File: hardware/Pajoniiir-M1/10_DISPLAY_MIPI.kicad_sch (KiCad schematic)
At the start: 30 parts

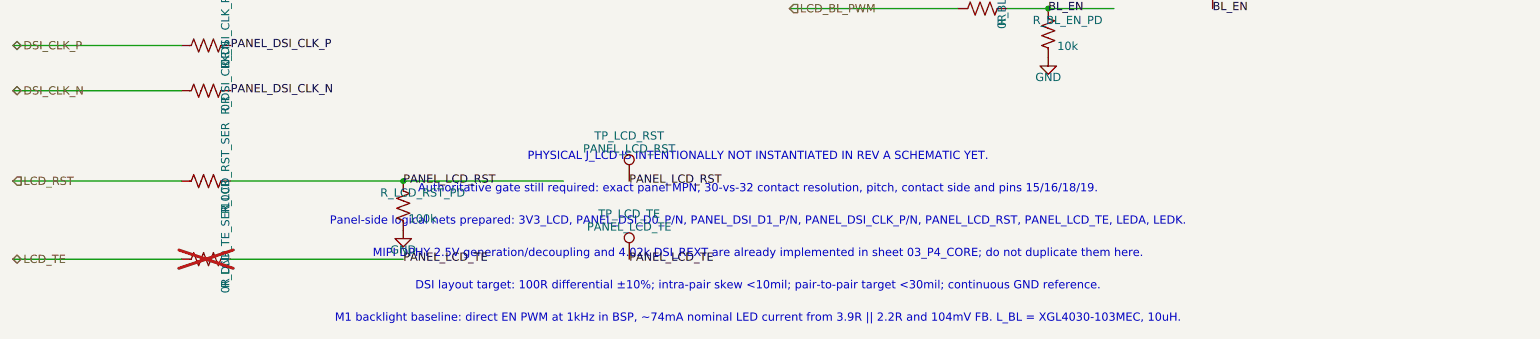
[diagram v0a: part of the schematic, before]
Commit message: hardware: record clean ERC and narrow display hard gate
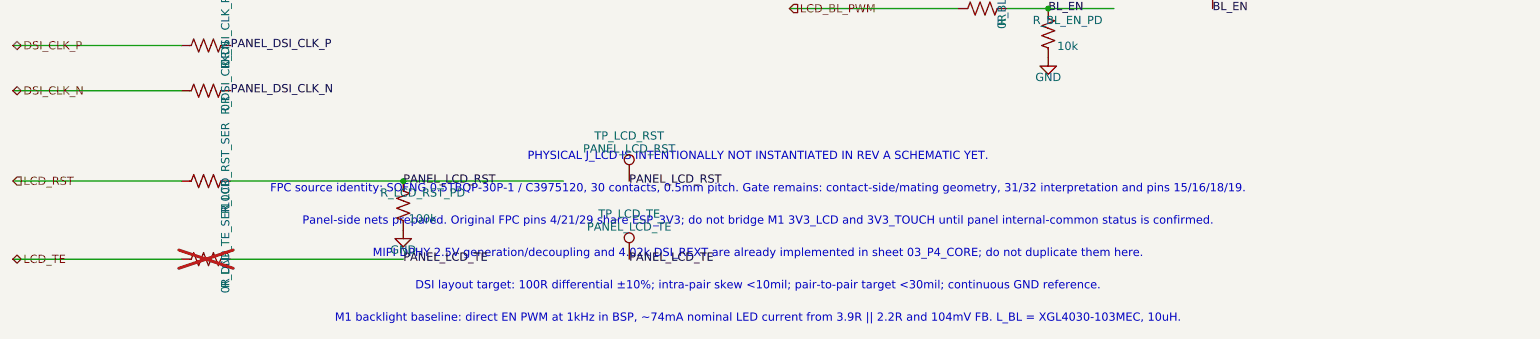
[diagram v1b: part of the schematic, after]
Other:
- note added: "FPC source identity: SOFNG 0.5TBQP-30P-1 / C3975120, 30 contacts, 0.5mm pitch. Gate remains: contact-side/mating geometry, 31/32 interpretation and pins 15/16/18/19."
- note added: "Panel-side nets prepared. Original FPC pins 4/21/29 share ESP_3V3; do not bridge M1 3V3_LCD and 3V3_TOUCH until panel internal-common status is confirmed."
- note removed: "Authoritative gate still required: exact panel MPN, 30-vs-32 contact resolution, pitch, contact side and pins 15/16/18/19."
- note removed: "Panel-side logical nets prepared: 3V3_LCD, PANEL_DSI_D0_P/N, PANEL_DSI_D1_P/N, PANEL_DSI_CLK_P/N, PANEL_LCD_RST, PANEL_LCD_TE, LEDA, LEDK."
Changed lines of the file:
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@@
   (label "BL_EN" (at 215.265 85.09 0) (effects (font (size 1.27 1.27))))
   (text "PHYSICAL J_LCD IS INTENTIONALLY NOT INSTANTIATED IN REV A SCHEMATIC YET." (exclude_from_sim no) (at 145 108 0) (effects (font (size 1.27 1.27))))
-  (text "Authoritative gate still required: exact panel MPN, 30-vs-32 contact resolution, pitch, contact side and pins 15/16/18/19." (exclude_from_sim no) (at 145 113 0) (effects (font (size 1.27 1.27))))
-  (text "Panel-side logical nets prepared: 3V3_LCD, PANEL_DSI_D0_P/N, PANEL_DSI_D1_P/N, PANEL_DSI_CLK_P/N, PANEL_LCD_RST, PANEL_LCD_TE, LEDA, LEDK." (exclude_from_sim no) (at 145 118 0) (effects (font (size 1.27 1.27))))
+  (text "FPC source identity: SOFNG 0.5TBQP-30P-1 / C3975120, 30 contacts, 0.5mm pitch. Gate remains: contact-side/mating geometry, 31/32 interpretation and pins 15/16/18/19." (exclude_from_sim no) (at 145 113 0) (effects (font (size 1.27 1.27))))
+  (text "Panel-side nets prepared. Original FPC pins 4/21/29 share ESP_3V3; do not bridge M1 3V3_LCD and 3V3_TOUCH until panel internal-common status is confirmed." (exclude_from_sim no) (at 145 118 0) (effects (font (size 1.27 1.27))))
   (text "MIPI DPHY 2.5V generation/decoupling and 4.02k DSI_REXT are already implemented in sheet 03_P4_CORE; do not duplicate them here." (exclude_from_sim no) (at 145 123 0) (effects (font (size 1.27 1.27))))
   (text "DSI layout target: 100R differential ±10%; intra-pair skew <10mil; pair-to-pair target <30mil; continuous GND reference." (exclude_from_sim no) (at 145 128 0) (effects (font (size 1.27 1.27))))

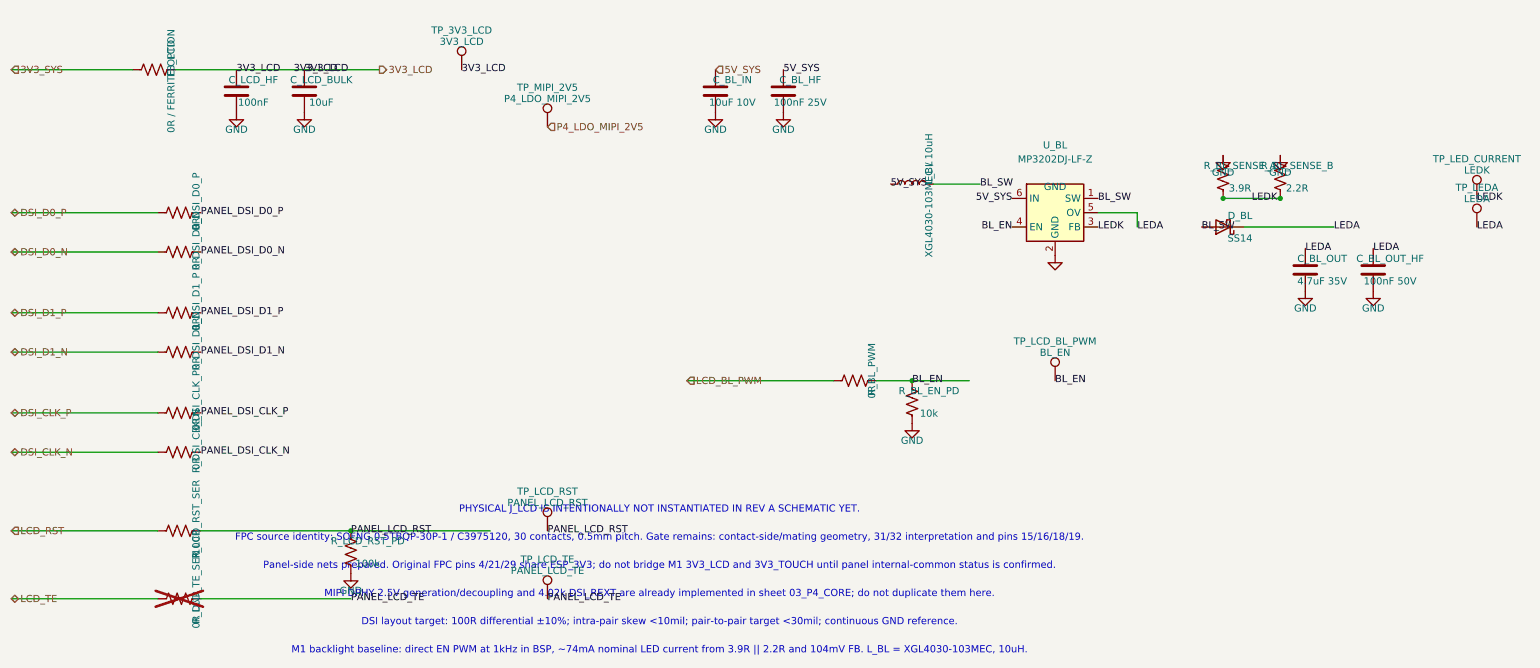
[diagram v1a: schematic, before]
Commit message: hardware: normalize schematic reference designators
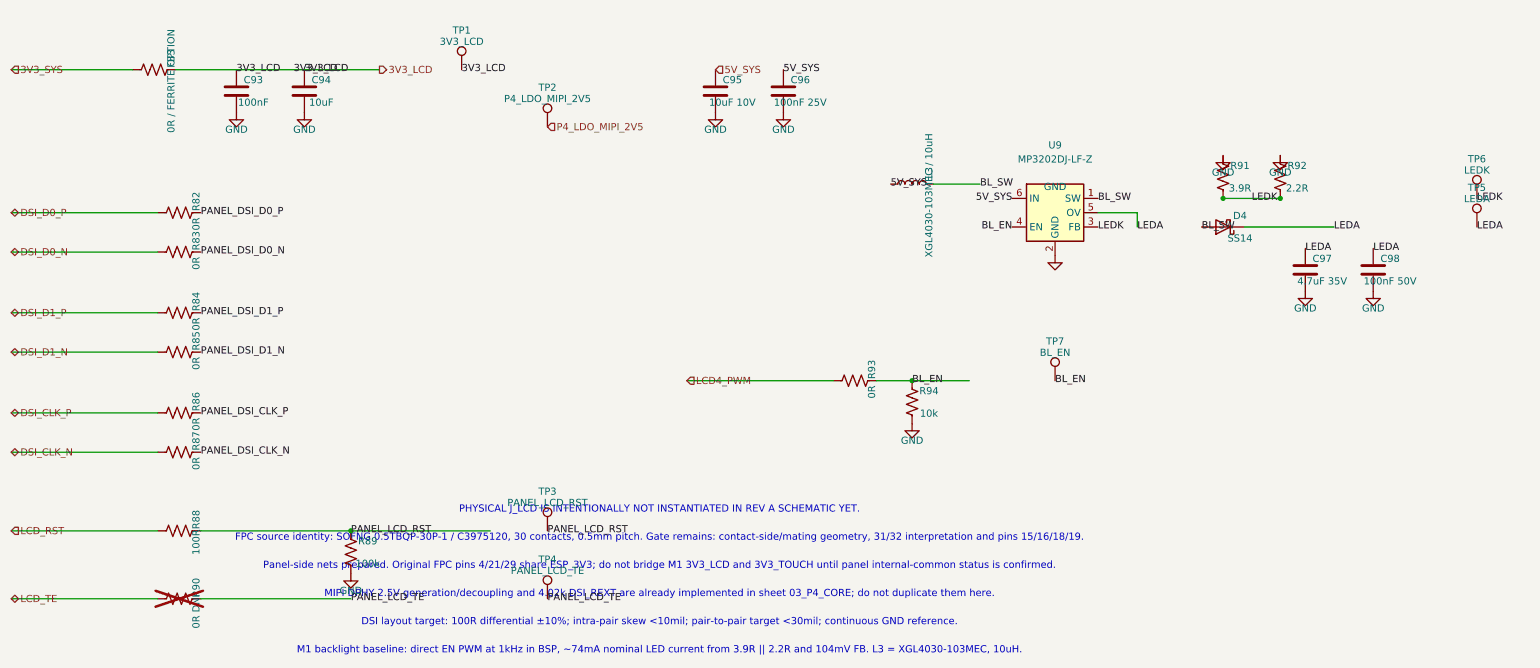
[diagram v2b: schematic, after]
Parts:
- renumbered C_LCD_HF to C93, C_LCD_BULK to C94, C_BL_IN to C95, C_BL_HF to C96, C_BL_OUT to C97, C_BL_OUT_HF to C98, D_BL to D4, FB_LCD to FB3, L_BL to L3, R_DSI_D0_P to R82, R_DSI_D0_N to R83, R_DSI_D1_P to R84, R_DSI_D1_N to R85, R_DSI_CLK_P to R86, R_DSI_CLK_N to R87, R_LCD_RST_SER to R88, R_LCD_RST_PD to R89, R_LCD_TE_SER to R90, R_BL_SENSE_A to R91, R_BL_SENSE_B to R92, R_BL_PWM to R93, R_BL_EN_PD to R94, TP_3V3_LCD to TP1, TP_MIPI_2V5 to TP2, TP_LCD_RST to TP3, TP_LCD_TE to TP4, TP_LEDA to TP5, TP_LED_CURRENT to TP6, TP_LCD_BL_PWM to TP7, U_BL to U9
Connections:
- net LCD_BL_PWM renamed LCD4_PWM
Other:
- note added: "M1 backlight baseline: direct EN PWM at 1kHz in BSP, ~74mA nominal LED current from 3.9R || 2.2R and 104mV FB. L3 = XGL4030-103MEC, 10uH."
- note removed: "M1 backlight baseline: direct EN PWM at 1kHz in BSP, ~74mA nominal LED current from 3.9R || 2.2R and 104mV FB. L_BL = XGL4030-103MEC, 10uH."

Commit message: hardware: constrain RefDes migration to annotation fields
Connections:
- net LCD4_PWM renamed LCD_BL_PWM
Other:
- note added: "M1 backlight baseline: direct EN PWM at 1kHz in BSP, ~74mA nominal LED current from 3.9R || 2.2R and 104mV FB. L_BL = XGL4030-103MEC, 10uH."
- note removed: "M1 backlight baseline: direct EN PWM at 1kHz in BSP, ~74mA nominal LED current from 3.9R || 2.2R and 104mV FB. L3 = XGL4030-103MEC, 10uH."
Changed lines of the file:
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@@
   )
   (label "LEDK" (at 290.195 52.705 0) (effects (font (size 1.27 1.27))))
-  (hierarchical_label "LCD4_PWM" (shape input) (at 149.86 85.09 0) (effects (font (size 1.27 1.27))))
+  (hierarchical_label "LCD_BL_PWM" (shape input) (at 149.86 85.09 0) (effects (font (size 1.27 1.27))))
   (symbol
     (lib_id "Device:R_US") (at 179.705 85.09 90) (unit 1)
@@
   (text "MIPI DPHY 2.5V generation/decoupling and 4.02k DSI_REXT are already implemented in sheet 03_P4_CORE; do not duplicate them here." (exclude_from_sim no) (at 145 123 0) (effects (font (size 1.27 1.27))))
   (text "DSI layout target: 100R differential ±10%; intra-pair skew <10mil; pair-to-pair target <30mil; continuous GND reference." (exclude_from_sim no) (at 145 128 0) (effects (font (size 1.27 1.27))))
-  (text "M1 backlight baseline: direct EN PWM at 1kHz in BSP, ~74mA nominal LED current from 3.9R || 2.2R and 104mV FB. L3 = XGL4030-103MEC, 10uH." (exclude_from_sim no) (at 145 133 0) (effects (font (size 1.27 1.27))))
+  (text "M1 backlight baseline: direct EN PWM at 1kHz in BSP, ~74mA nominal LED current from 3.9R || 2.2R and 104mV FB. L_BL = XGL4030-103MEC, 10uH." (exclude_from_sim no) (at 145 133 0) (effects (font (size 1.27 1.27))))
   (sheet_instances (path "/" (page "11")))
   (embedded_fonts no)
